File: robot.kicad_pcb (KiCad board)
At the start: 2 copper layers, 55.2 x 92.1 mm, 63 parts, among them J1 PCA9865 2, J10 BATT out, J2 I2S, J3 Programming, J4 IMU, J5 Switches, J6 Expansion, J7 VCC, J8 Servo pwr, J9 BATT in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

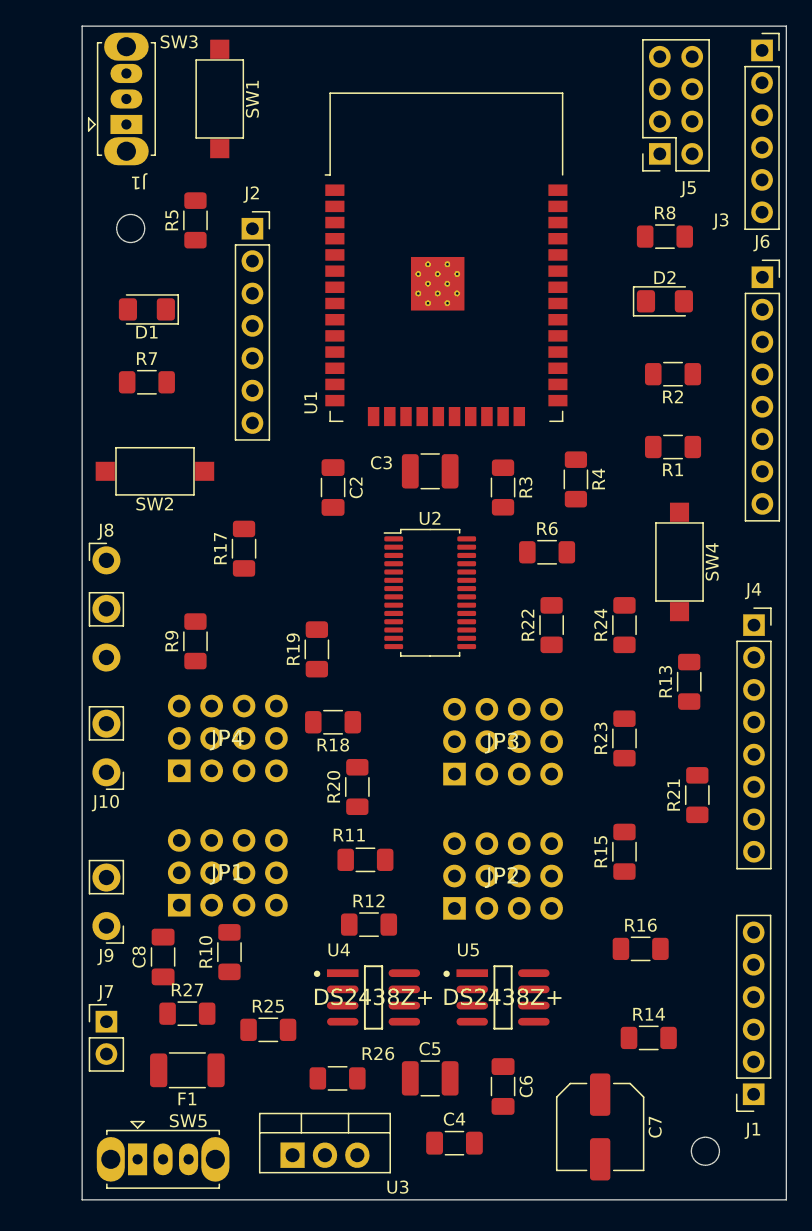
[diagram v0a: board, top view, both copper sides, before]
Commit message: Added extra mounting hole
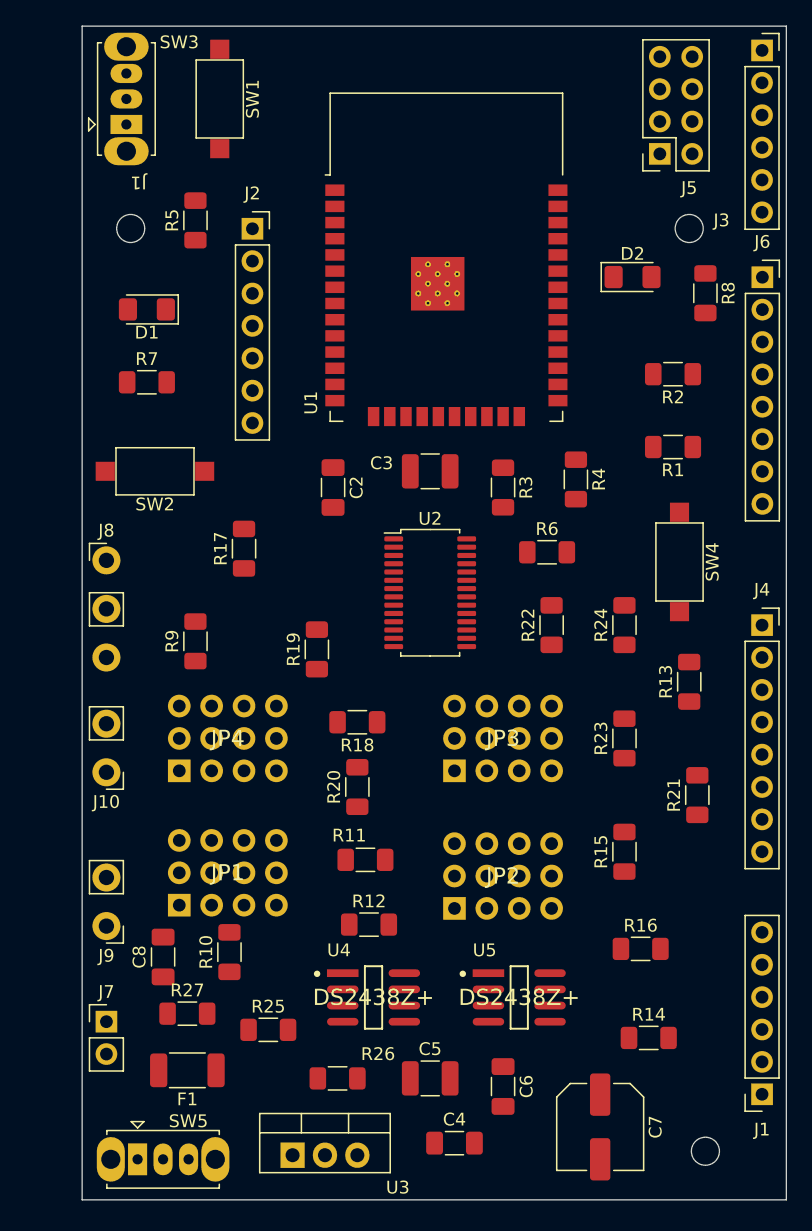
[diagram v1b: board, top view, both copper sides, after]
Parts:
- added REF**: MountingHole_2.2mm_M2, MountingHole:MountingHole_2.2mm_M2, F.Cu at (143.5, 111.8)
- moved R8 5.46 mm to (144.8, 116.8), turned to -90 degrees
- moved D2 3.17 mm to (139.1, 115.6)
- moved R18 1.91 mm to (117.5, 150.5)
- moved U5 1.27 mm to (130.2, 172.1)
- moved J1 0.66 mm to (149.2, 179.7)
- moved J4 0.63 mm to (149.2, 142.9)
- moved JP3 0.25 mm to (128.9, 151.8)
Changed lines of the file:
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@@
   )
   (footprint "DS2438:Maxim-S8-5-0-P-IPC_A" (layer "F.Cu")
-    (at 128.905 172.085)
+    (at 130.175 172.085)
     (property "Sheetfile" "power_mointoring.kicad_sch")
     (property "Sheetname" "Power monitoring")
@@
   )
   (footprint "Resistor_SMD:R_1206_3216Metric_Pad1.30x1.75mm_HandSolder" (layer "F.Cu")
-    (at 141.605 112.395)
+    (at 144.78 116.84 -90)
     (descr "Resistor SMD 1206 (3216 Metric), square (rectangular) end terminal, IPC_7351 nominal with elongated pad for handsoldering. (Body size source: IPC-SM-782 page 72, https://www.pcb-3d.com/wordpress/wp-content/uploads/ipc-sm-782a_amendment_1_and_2.pdf), generated with kicad-footprint-generator")
     (tags "resistor handsolder")
@@
     (property "Sheetname" "")
     (attr smd)
-    (fp_text reference "R8" (at 0 -1.82) (layer "F.SilkS")
-      (effects (font (size 1 1) (thickness 0.15)))
-    )
-    (fp_text value "470" (at 0 1.82) (layer "F.Fab")
-      (effects (font (size 1 1) (thickness 0.15)))
-    )
-    (fp_text user "${REFERENCE}" (at 0 0) (layer "F.Fab")
+    (fp_text reference "R8" (at 0 -1.82 90) (layer "F.SilkS")
+      (effects (font (size 1 1) (thickness 0.15)))
+    )
+    (fp_text value "470" (at 0 1.82 90) (layer "F.Fab")
+      (effects (font (size 1 1) (thickness 0.15)))
+    )
+    (fp_text user "${REFERENCE}" (at 0 0 90) (layer "F.Fab")
       (effects (font (size 0.8 0.8) (thickness 0.12)))
     )
@@
     (fp_line (start -1.6 0.8) (end -1.6 -0.8) (layer "F.Fab") (width 0.1))
     (fp_line (start 1.6 0.8) (end -1.6 0.8) (layer "F.Fab") (width 0.1))
-    (pad "1" smd roundrect (at -1.55 0) (size 1.3 1.75) (layers "F.Cu" "F.Paste" "F.Mask") (roundrect_rratio 0.192308)
+    (pad "1" smd roundrect (at -1.55 0 270) (size 1.3 1.75) (layers "F.Cu" "F.Paste" "F.Mask") (roundrect_rratio 0.192308)
       (net 1 "GND") (pintype "passive"))
-    (pad "2" smd roundrect (at 1.55 0) (size 1.3 1.75) (layers "F.Cu" "F.Paste" "F.Mask") (roundrect_rratio 0.192308)
+    (pad "2" smd roundrect (at 1.55 0 270) (size 1.3 1.75) (layers "F.Cu" "F.Paste" "F.Mask") (roundrect_rratio 0.192308)
       (net 11 "Net-(D2-Pad2)") (pintype "passive"))
     (model "${KICAD6_3DMODEL_DIR}/Resistor_SMD.3dshapes/R_1206_3216Metric.wrl"
@@
   )
   (footprint "Connector_PinSocket_2.54mm:PinSocket_1x06_P2.54mm_Vertical" (layer "F.Cu")
-    (at 148.565 179.68 180)
+    (at 149.225 179.68 180)
     (descr "Through hole straight socket strip, 1x06, 2.54mm pitch, single row (from Kicad 4.0.7), script generated")
     (tags "Through hole socket strip THT 1x06 2.54mm single row")
@@
   )
   (footprint "Adafruit:3X04" (layer "F.Cu")
-    (at 128.905 152.019)
+    (at 128.905 151.765)
     (property "Sheetfile" "robot.kicad_sch")
     (property "Sheetname" "")
@@
   )
   (footprint "Connector_PinSocket_2.54mm:PinSocket_1x08_P2.54mm_Vertical" (layer "F.Cu")
-    (at 148.59 142.875)
+    (at 149.225 142.875)
     (descr "Through hole straight socket strip, 1x08, 2.54mm pitch, single row (from Kicad 4.0.7), script generated")
     (tags "Through hole socket strip THT 1x08 2.54mm single row")
@@
   )
   (footprint "Resistor_SMD:R_1206_3216Metric_Pad1.30x1.75mm_HandSolder" (layer "F.Cu")
-    (at 115.57 150.495 180)
+    (at 117.475 150.495 180)
     (descr "Resistor SMD 1206 (3216 Metric), square (rectangular) end terminal, IPC_7351 nominal with elongated pad for handsoldering. (Body size source: IPC-SM-782 page 72, https://www.pcb-3d.com/wordpress/wp-content/uploads/ipc-sm-782a_amendment_1_and_2.pdf), generated with kicad-footprint-generator")
     (tags "resistor handsolder")
@@
       (rotate (xyz 0 0 0))
     )
+  )
+  (footprint "MountingHole:MountingHole_2.2mm_M2" (layer "F.Cu")
+    (at 143.51 111.76)
+    (descr "Mounting Hole 2.2mm, no annular, M2")
+    (tags "mounting hole 2.2mm no annular m2")
+    (attr exclude_from_pos_files exclude_from_bom)
+    (fp_text reference "REF**" (at 0 -3.2) (layer "F.SilkS") hide
+      (effects (font (size 1 1) (thickness 0.15)))
+    )
+    (fp_text value "MountingHole_2.2mm_M2" (at 0 3.2) (layer "F.Fab") hide
+      (effects (font (size 1 1) (thickness 0.15)))
+    )
+    (fp_text user "${REFERENCE}" (at 0 0) (layer "F.Fab")
+      (effects (font (size 1 1) (thickness 0.15)))
+    )
+    (fp_circle (center 0 0) (end 2.2 0) (layer "Cmts.User") (width 0.15) (fill none))
+    (fp_circle (center 0 0) (end 2.45 0) (layer "F.CrtYd") (width 0.05) (fill none))
+    (pad "" np_thru_hole circle (at 0 0) (size 2.2 2.2) (drill 2.2) (layers F&B.Cu *.Mask))
   )
   (footprint "Button_Switch_THT:SW_Slide_1P2T_CK_OS102011MS2Q" (layer "F.Cu")
@@
   )
   (footprint "LED_SMD:LED_1206_3216Metric_Pad1.42x1.75mm_HandSolder" (layer "F.Cu")
-    (at 141.605 117.475)
+    (at 139.065 115.57)
     (descr "LED SMD 1206 (3216 Metric), square (rectangular) end terminal, IPC_7351 nominal, (Body size source: http://www.tortai-tech.com/upload/download/2011102023233369053.pdf), generated with kicad-footprint-generator")
     (tags "LED handsolder")

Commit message: Ready to route.
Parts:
- moved J10 41.2 mm to (125.0, 185.4), turned to 90 degrees
- moved C4 2.50 mm to (123.5, 181.6)
- moved C6 2.05 mm to (130.2, 177.5), turned to 90 degrees
- moved C5 1.60 mm to (124.2, 177.2)
- moved U4 0.64 mm to (118.7, 171.4)
- moved U5 0.64 mm to (130.2, 171.4)
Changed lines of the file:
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@@
   )
   (setup
+    (stackup
+      (layer "F.SilkS" (type "Top Silk Screen"))
+      (layer "F.Paste" (type "Top Solder Paste"))
+      (layer "F.Mask" (type "Top Solder Mask") (thickness 0.01))
+      (layer "F.Cu" (type "copper") (thickness 0.035))
+      (layer "dielectric 1" (type "core") (thickness 1.51) (material "FR4") (epsilon_r 4.5) (loss_tangent 0.02))
+      (layer "B.Cu" (type "copper") (thickness 0.035))
+      (layer "B.Mask" (type "Bottom Solder Mask") (thickness 0.01))
+      (layer "B.Paste" (type "Bottom Solder Paste"))
+      (layer "B.SilkS" (type "Bottom Silk Screen"))
+      (copper_finish "None")
+      (dielectric_constraints no)
+    )
     (pad_to_mask_clearance 0)
     (pcbplotparams
@@
   )
   (footprint "DS2438:Maxim-S8-5-0-P-IPC_A" (layer "F.Cu")
-    (at 130.175 172.085)
+    (at 130.175 171.45)
     (property "Sheetfile" "power_mointoring.kicad_sch")
     (property "Sheetname" "Power monitoring")
@@
   )
   (footprint "DS2438:Maxim-S8-5-0-P-IPC_A" (layer "F.Cu")
-    (at 118.745 172.085)
+    (at 118.745 171.45)
     (property "Sheetfile" "power_mointoring.kicad_sch")
     (property "Sheetname" "Power monitoring")
@@
   )
   (footprint "Capacitor_SMD:C_1206_3216Metric_Pad1.33x1.80mm_HandSolder" (layer "F.Cu")
-    (at 128.905 179.07 -90)
+    (at 130.175 177.4575 90)
     (descr "Capacitor SMD 1206 (3216 Metric), square (rectangular) end terminal, IPC_7351 nominal with elongated pad for handsoldering. (Body size source: IPC-SM-782 page 76, https://www.pcb-3d.com/wordpress/wp-content/uploads/ipc-sm-782a_amendment_1_and_2.pdf), generated with kicad-footprint-generator")
     (tags "capacitor handsolder")
@@
     (fp_line (start -1.6 -0.8) (end 1.6 -0.8) (layer "F.Fab") (width 0.1))
     (fp_line (start 1.6 0.8) (end -1.6 0.8) (layer "F.Fab") (width 0.1))
-    (pad "1" smd roundrect (at -1.5625 0 270) (size 1.325 1.8) (layers "F.Cu" "F.Paste" "F.Mask") (roundrect_rratio 0.188679)
+    (pad "1" smd roundrect (at -1.5625 0 90) (size 1.325 1.8) (layers "F.Cu" "F.Paste" "F.Mask") (roundrect_rratio 0.188679)
       (net 2 "VCC") (pintype "passive"))
-    (pad "2" smd roundrect (at 1.5625 0 270) (size 1.325 1.8) (layers "F.Cu" "F.Paste" "F.Mask") (roundrect_rratio 0.188679)
+    (pad "2" smd roundrect (at 1.5625 0 90) (size 1.325 1.8) (layers "F.Cu" "F.Paste" "F.Mask") (roundrect_rratio 0.188679)
       (net 1 "GND") (pintype "passive"))
     (model "${KICAD6_3DMODEL_DIR}/Capacitor_SMD.3dshapes/C_1206_3216Metric.wrl"
@@
   )
   (footprint "Capacitor_SMD:C_1206_3216Metric_Pad1.33x1.80mm_HandSolder" (layer "F.Cu")
-    (at 125.095 183.515)
+    (at 123.4825 181.61)
     (descr "Capacitor SMD 1206 (3216 Metric), square (rectangular) end terminal, IPC_7351 nominal with elongated pad for handsoldering. (Body size source: IPC-SM-782 page 76, https://www.pcb-3d.com/wordpress/wp-content/uploads/ipc-sm-782a_amendment_1_and_2.pdf), generated with kicad-footprint-generator")
     (tags "capacitor handsolder")
@@
     (property "Sheetname" "Power monitoring")
     (attr smd)
-    (fp_text reference "C4" (at 0 -1.85) (layer "F.SilkS")
-      (effects (font (size 1 1) (thickness 0.15)))
-    )
-    (fp_text value "104" (at 0 1.85) (layer "F.Fab")
+    (fp_text reference "C4" (at -2.1975 1.905) (layer "F.SilkS")
+      (effects (font (size 1 1) (thickness 0.15)))
+    )
+    (fp_text value "104" (at 4.1525 -0.635) (layer "F.Fab")
       (effects (font (size 1 1) (thickness 0.15)))
     )
@@
   )
   (footprint "Capacitor_SMD:C_1210_3225Metric_Pad1.33x2.70mm_HandSolder" (layer "F.Cu")
-    (at 123.19 178.435)
+    (at 124.1675 177.165)
     (descr "Capacitor SMD 1210 (3225 Metric), square (rectangular) end terminal, IPC_7351 nominal with elongated pad for handsoldering. (Body size source: IPC-SM-782 page 76, https://www.pcb-3d.com/wordpress/wp-content/uploads/ipc-sm-782a_amendment_1_and_2.pdf), generated with kicad-footprint-generator")
     (tags "capacitor handsolder")
@@
     (property "Sheetname" "Power monitoring")
     (attr through_hole)
-    (fp_text reference "SW5" (at 3.99 -2.99) (layer "F.SilkS")
-      (effects (font (size 1 1) (thickness 0.15)))
-    )
-    (fp_text value "POWER" (at 2 3) (layer "F.Fab")
-      (effects (font (size 1 1) (thickness 0.15)))
-    )
-    (fp_text user "${REFERENCE}" (at 3.99 -2.99) (layer "F.Fab")
+    (fp_text reference "SW5" (at 8.985 2.54) (layer "F.SilkS")
+      (effects (font (size 1 1) (thickness 0.15)))
+    )
+    (fp_text value "POWER" (at 5.81 -3.175) (layer "F.Fab")
+      (effects (font (size 1 1) (thickness 0.15)))
+    )
+    (fp_text user "${REFERENCE}" (at -1.81 -3.175) (layer "F.Fab")
       (effects (font (size 1 1) (thickness 0.15)))
     )
@@
   )
   (footprint "Connector_PinHeader_2.54mm:Connector_Battery_SolderPads" (layer "F.Cu")
-    (at 97.79 154.421 180)
+    (at 124.979 185.42 90)
     (descr "Through hole straight pin header, 1x02, 2.54mm pitch, single row")
     (tags "Through hole pin header THT 1x02 2.54mm single row")
@@
     (property "Sheetname" "Power monitoring")
     (attr through_hole)
-    (fp_text reference "J10" (at 0 -2.33) (layer "F.SilkS")
-      (effects (font (size 1 1) (thickness 0.15)))
-    )
-    (fp_text value "BATT out" (at -2.54 2.54 90) (layer "F.Fab")
-      (effects (font (size 1 1) (thickness 0.15)))
-    )
-    (fp_text user "${REFERENCE}" (at 0 2.54 90) (layer "F.Fab")
+    (fp_text reference "J10" (at 0 -2.33 90) (layer "F.SilkS")
+      (effects (font (size 1 1) (thickness 0.15)))
+    )
+    (fp_text value "BATT out" (at -1.905 9.006) (layer "F.Fab")
+      (effects (font (size 1 1) (thickness 0.15)))
+    )
+    (fp_text user "${REFERENCE}" (at 0 2.54) (layer "F.Fab")
       (effects (font (size 1 1) (thickness 0.15)))
     )
@@
     (fp_line (start -1.27 -0.635) (end -0.635 -1.27) (layer "F.Fab") (width 0.1))
     (fp_line (start -0.635 -1.27) (end 1.27 -1.27) (layer "F.Fab") (width 0.1))
-    (pad "1" thru_hole circle (at 0 0 180) (size 2.2 2.2) (drill 1.2) (layers *.Cu *.Mask)
+    (pad "1" thru_hole circle (at 0 0 90) (size 2.2 2.2) (drill 1.2) (layers *.Cu *.Mask)
       (net 3 "+BATT") (pinfunction "Pin_1") (pintype "passive"))
-    (pad "2" thru_hole circle (at 0 3.81 180) (size 2.2 2.2) (drill 1.2) (layers *.Cu *.Mask)
+    (pad "2" thru_hole circle (at 0 3.81 90) (size 2.2 2.2) (drill 1.2) (layers *.Cu *.Mask)
       (net 1 "GND") (pinfunction "Pin_2") (pintype "passive"))
     (model "${KICAD6_3DMODEL_DIR}/Connector_PinHeader_2.54mm.3dshapes/PinHeader_1x02_P2.54mm_Vertical.wrl"
@@
       (effects (font (size 1 1) (thickness 0.15)))
     )
-    (fp_text value "2.6A 12V" (at 5.715 -2.54) (layer "F.Fab")
-      (effects (font (size 1 1) (thickness 0.15)))
-    )
+    (fp_text value "2.6A 12V" (at -4.445 -2.54) (layer "F.Fab")
+      (effects (font (size 1 1) (thickness 0.15)))
+    )

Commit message: Ready for fab.
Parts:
- added C1: 104, Capacitor_SMD:C_1206_3216Metric_Pad1.33x1.80mm_HandSolder, F.Cu at (112.8, 113.4)
- added REF**: MountingHole_2.2mm_M2, MountingHole:MountingHole_2.2mm_M2, F.Cu at (99.8, 139.4)
- added TP1: ONEWIRE_BUS, TestPoint:TestPoint_Pad_D2.0mm, F.Cu at (124.8, 166.2)
- moved R27 43.7 mm to (112.5, 130.4)
- moved JP4 26.0 mm to (133.3, 151.6), turned to 180 degrees
- moved R14 24.9 mm to (141.2, 150.3), turned to 90 degrees
- moved R9 24.9 mm to (124.2, 159.8), turned to 180 degrees
- moved JP3 21.5 mm to (107.4, 151.6), turned to 180 degrees
- moved R16 19.8 mm to (124.2, 156.0), turned to 180 degrees
- moved R13 18.8 mm to (124.7, 148.2), turned to 180 degrees
- moved R12 16.1 mm to (105.2, 157.1)
- moved R18 14.9 mm to (107.2, 139.7), turned to 0 degrees
- moved R10 13.0 mm to (117.1, 159.8), turned to 0 degrees
- moved J8 12.6 mm to (97.8, 150.4)
- moved R21 12.5 mm to (141.2, 144.0)
- moved R20 11.7 mm to (113.1, 144.8), turned to 0 degrees
- moved R19 10.9 mm to (103.4, 145.3), turned to 0 degrees
- moved R23 10.7 mm to (134.8, 141.7), turned to 180 degrees
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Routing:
- net GND: track 0.00 -> 454.2 mm, vias 0 -> 12
- net VCC: track 0.00 -> 243.9 mm, vias 0 -> 2
- net /WIRE_1_SCL: track 0.00 -> 91.7 mm, vias 0 -> 3
- net /WIRE_1_SDA: track 0.00 -> 75.8 mm, vias 0 -> 3
- net +5V: track 0.00 -> 65.9 mm, vias 0 -> 2
- net ONEWIRE_BUS: track 0.00 -> 64.7 mm, vias 0 -> 3
- net +5VD: track 0.00 -> 59.4 mm, vias 0 -> 1
- net +BATT: track 0.00 -> 49.9 mm, vias 0 -> 2
- net /WIRE_0_SCL: track 0.00 -> 49.4 mm, vias 0 -> 1
- net /WIRE_0_SDA: track 0.00 -> 41.8 mm, vias 0 -> 3
- net /PWM3: track 0.00 -> 40.7 mm, vias 0 -> 2
- net /IO_34: track 0.00 -> 39.3 mm, vias 0 -> 3
- net /IO_35: track 0.00 -> 38.7 mm, vias 0 -> 1
- net /IO_32: track 0.00 -> 38.4 mm, vias 0 -> 2
- net Net-(SW3-Pad1): track 0.00 -> 32.6 mm, vias 0 -> 1
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- added copper zone on B.Cu, net GND
- added copper zone on F.Cu, net GND
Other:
- board size 55.2 x 92.1 mm -> 55.2 x 89.3 mm
- board text added: "PWM +VA GND"
- board text added: "PWM +VB GND"
